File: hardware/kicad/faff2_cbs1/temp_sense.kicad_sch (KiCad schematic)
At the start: 40 parts, among them J701 1752120, J702 1752120, J703 8510-4500PL, U701 ADS1120

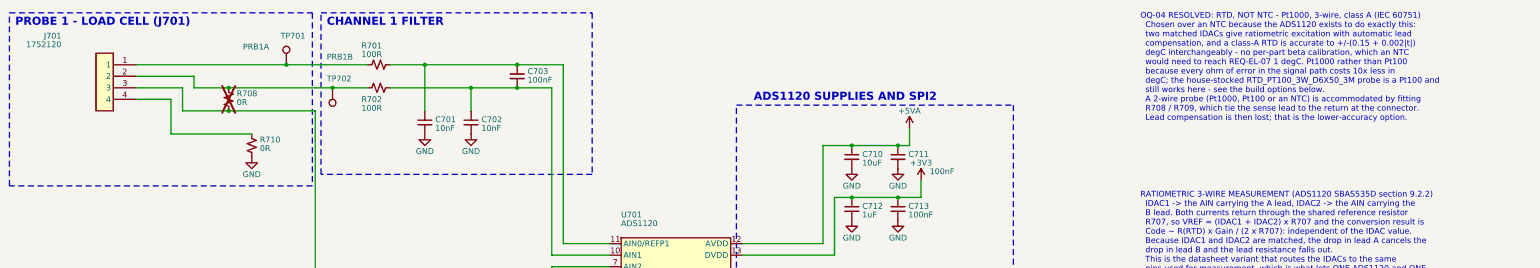
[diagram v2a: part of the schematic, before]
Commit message: review r4 items 2,3,5,6,9: PGND, the frame boundary, and the U.FL connectors
Item 2, U304's PGND ground sitting on top of C318: the answer was already on
the sheet. U301 is the same regulator wired the same way, and its PGND ground
hangs 1.27 mm below the pin with its name clear above the VCC stub; U304's hung
6.35 mm down, which put it in C318's lane. Making it match U301 also closes both
of round 3's residual findings - power_rails is clear for the first time.

Item 3, the +5VA symbol outside the sheet boundary: the drawing area starts at
y=11.94, measured off a render, and the "+5VA" name's box ran 10.79..12.06 -
straddling it, inside the frame's ruler band. The whole excitation cluster drops
6.35 mm, the block box follows, and the feed keeps its long run and doglegs down
to the new row.

Item 9 is the same defect: temp_sense's PROBE 1 and CHANNEL 1 FILTER rectangles
start at y=11.43, half a millimetre above the drawing area. So do four of mcu's,
laid out to the same wrong value, so both sheets are fixed - every top edge to
12.70 and the titles under them to 13.34. Nothing on any sheet is above the
boundary now.

Item 5, FL501/FL502 -> J503/J504. The captain is right and there is no reason
that survives: they are Amodo_Connectors:CONUFL001-SMD, U.FL coaxial
connectors, with connector footprints, and the library symbol's own default
reference prefix is J. The FL prefix was an instance-level override
contradicting the part, and in IEEE-315 FL designates a filter. They sit in a
filter chain, which is the only reading that explains it. DEC-A14 records it.

Item 6, a concise pin-out beside J501. The full table was in the notes column
90 mm away; this is the five-line version directly under the connector, where
somebody landing a cable will look. Width is capped by the signal wires
dropping at x=48.26.

ERC 0/0 at severity-all; 408 components, 264 nets. The only netlist change is
item 5's re-designation - same nets, same members, new names.

Co-Authored-By: Claude Opus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
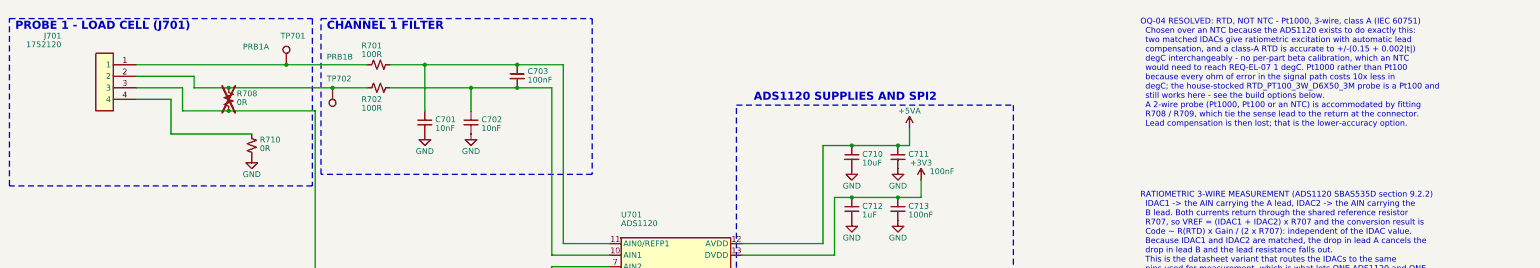
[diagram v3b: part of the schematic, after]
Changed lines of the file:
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@@
 	)
 	(rectangle
-		(start 17.78 11.43)
+		(start 17.78 12.7)
 		(end 84.46 49.53)
 		(stroke
@@
 		"PROBE 1 - LOAD CELL (J701)"
 		(exclude_from_sim no)
-		(at 19.05 12.45 0)
+		(at 19.05 13.34 0)
 		(effects
 			(font
@@
 	)
 	(rectangle
-		(start 86.36 11.43)
+		(start 86.36 12.7)
 		(end 146.05 46.99)
 		(stroke
@@
 		"CHANNEL 1 FILTER"
 		(exclude_from_sim no)
-		(at 87.63 12.45 0)
+		(at 87.63 13.34 0)
 		(effects
 			(font
@@
 		"OQ-04 RESOLVED: RTD, NOT NTC - Pt1000, 3-wire, class A (IEC 60751)\n  Chosen over an NTC because the ADS1120 exists to do exactly this:\n  two matched IDACs give ratiometric excitation with automatic lead\n  compensation, and a class-A RTD is accurate to +/-(0.15 + 0.002|t|)\n  degC interchangeably - no per-part beta calibration, which an NTC\n  would need to reach REQ-EL-07 1 degC. Pt1000 rather than Pt100\n  because every ohm of error in the signal path costs 10x less in\n  degC; the house-stocked RTD_PT100_3W_D6X50_3M probe is a Pt100 and\n  still works here - see the build options below.\n  A 2-wire probe (Pt1000, Pt100 or an NTC) is accommodated by fitting\n  R708 / R709, which tie the sense lead to the return at the connector.\n  Lead compensation is then lost; that is the lower-accuracy option."
 		(exclude_from_sim no)
-		(at 266.7 11.43 0)
+		(at 266.7 12.7 0)
 		(effects
 			(font
